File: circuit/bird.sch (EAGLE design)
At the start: 24 parts, among them J1 22-27-2031-03, U1 ATTINY84-20SSU, X1 MINI-USB-32005-201

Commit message: remove opamp circuit
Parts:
- removed C5: 220pf, rcl:C-USC0603
- removed R2: 47k, rcl:R-US_R0603
- removed R3: 10M, rcl:R-US_R0603
- removed R4: 90k, rcl:R-US_R0603
- removed R5: 100k, rcl:R-US_R0603
- removed TP1: TEST-POINT2, SparkFun:TEST-POINT2
- removed U$5: MCP601, SparkFun:MCP601
- removed X1: MINI-USB-32005-201, con-cypressindustries:MINI-USB-32005-201
- added BATTERY: M02JST-PTH-2, SparkFun-Connectors:M02JST-PTH-2
- added PAD1: (no value), wirepad:2,54/0,8
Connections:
- removed net D+: X1.3
- removed net D-: X1.2
- removed net MAGNETIC_SENSOR_IN: J1-3.S, R2.1
- removed net N$4: C5.1, R2.2, R3.2, U$5.V-
- removed net N$5: R4.1, R5.2, U$5.V+
- net 5V: now also BATTERY.1; no longer R1.2, R4.2, U$5.VDD, X1.1
- net GND: now also BATTERY.2, R1.1; no longer R5.1, U$5.VSS, X1.5
- net INDICATOR: now also LED1.A; no longer LED1.C
- net MAGNETIC_REFERENCE: now also PAD1.P; no longer TP1.1
- net MAGNETIC_SENSOR: now also J1-3.S; no longer C5.2, R3.1, U$5.VOUT
- net N$1: now also LED1.C, R1.2; no longer LED1.A, R1.1
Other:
- note removed: "Inverting Amplifier"
- note removed: "Linear Hall Effect Sensor"
- note removed: "Low pass filter"
- note removed: "Voltage Divider Provides reference voltage"
- moved on the sheet: LED1

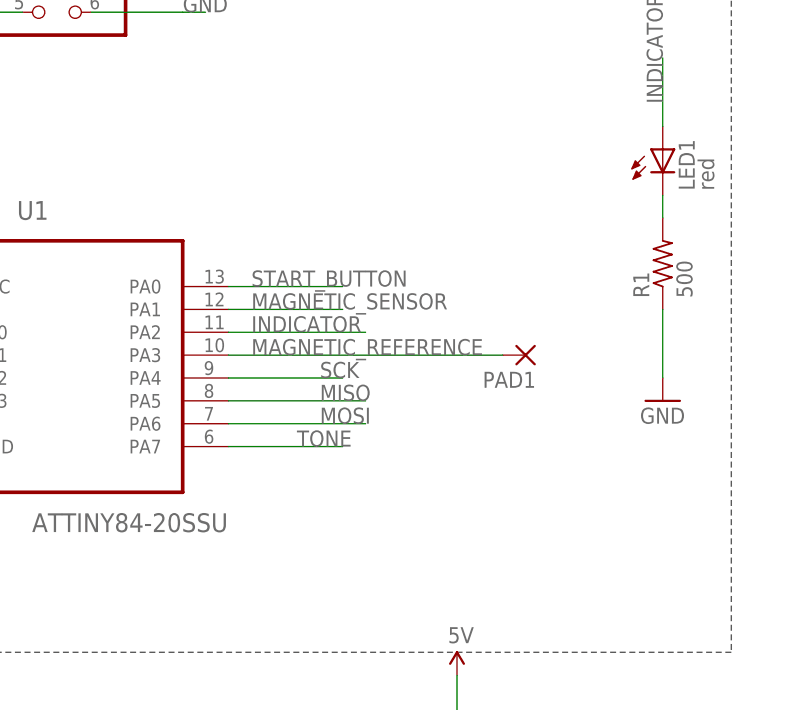
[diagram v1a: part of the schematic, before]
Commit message: add pads for resistors
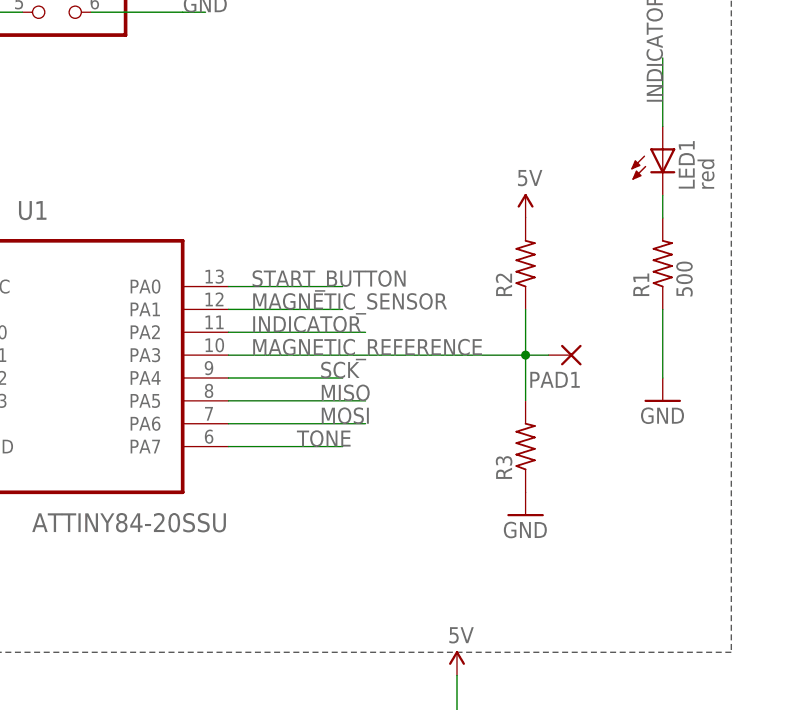
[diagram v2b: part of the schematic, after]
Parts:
- added R2, R3: (no value), rcl:R-US_R0603
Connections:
- net 5V: now also R2.2
- net GND: now also R3.1
- net MAGNETIC_REFERENCE: now also R2.1, R3.2
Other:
- moved on the sheet: PAD1
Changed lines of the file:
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@@
 <part name="SUPPLY2" library="SparkFun-Aesthetics" deviceset="5V" device=""/>
 <part name="GND10" library="SparkFun-Aesthetics" deviceset="GND" device=""/>
+<part name="R2" library="rcl" deviceset="R-US_" device="R0603"/>
+<part name="R3" library="rcl" deviceset="R-US_" device="R0603"/>
+<part name="SUPPLY3" library="SparkFun-Aesthetics" deviceset="5V" device=""/>
+<part name="GND11" library="SparkFun-Aesthetics" deviceset="GND" device=""/>
 </parts>
 <sheets>
@@
 <instance part="GND12" gate="1" x="-203.2" y="15.24"/>
 <instance part="SG2" gate="G$1" x="127" y="-35.56" rot="MR90"/>
-<instance part="PAD1" gate="P" x="53.34" y="40.64" rot="R180"/>
+<instance part="PAD1" gate="P" x="58.42" y="40.64" rot="R180"/>
 <instance part="GND8" gate="1" x="68.58" y="35.56"/>
 <instance part="BATTERY" gate="G$1" x="-38.1" y="-22.86" rot="R90"/>
 <instance part="SUPPLY2" gate="G$1" x="-38.1" y="-7.62"/>
 <instance part="GND10" gate="1" x="-55.88" y="-22.86"/>
+<instance part="R2" gate="G$1" x="53.34" y="50.8" rot="R90"/>
+<instance part="R3" gate="G$1" x="53.34" y="30.48" rot="R90"/>
+<instance part="SUPPLY3" gate="G$1" x="53.34" y="55.88"/>
+<instance part="GND11" gate="1" x="53.34" y="22.86"/>
 </instances>
 <busses>
@@
 <pinref part="SUPPLY2" gate="G$1" pin="5V"/>
 </segment>
+<segment>
+<pinref part="R2" gate="G$1" pin="2"/>
+<pinref part="SUPPLY3" gate="G$1" pin="5V"/>
+</segment>
 </net>
 <net name="GND" class="0">
@@
 <junction x="-55.88" y="-20.32"/>
 </segment>
+<segment>
+<pinref part="R3" gate="G$1" pin="1"/>
+<pinref part="GND11" gate="1" pin="GND"/>
+</segment>
 </net>
 <net name="TONE" class="0">
@@
 <segment>
 <pinref part="U1" gate="A" pin="PA3"/>
-<wire x1="20.32" y1="40.64" x2="50.8" y2="40.64" width="0.1524" layer="91"/>
+<wire x1="20.32" y1="40.64" x2="53.34" y2="40.64" width="0.1524" layer="91"/>
 <label x="22.86" y="40.64" size="1.778" layer="95"/>
 <pinref part="PAD1" gate="P" pin="P"/>
-</segment>
-</net>
+<pinref part="R2" gate="G$1" pin="1"/>
+<wire x1="53.34" y1="40.64" x2="55.88" y2="40.64" width="0.1524" layer="91"/>
+<wire x1="53.34" y1="45.72" x2="53.34" y2="40.64" width="0.1524" layer="91"/>
+<junction x="53.34" y="40.64"/>
+<pinref part="R3" gate="G$1" pin="2"/>
+<wire x1="53.34" y1="35.56" x2="53.34" y2="40.64" width="0.1524" layer="91"/>
+</segment>
+</net>
